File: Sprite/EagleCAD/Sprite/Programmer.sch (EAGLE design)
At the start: 5 parts

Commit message: Programmer Board
Finished programmer shield board
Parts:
- added JP5: (no value), SparkFun:M03LOCK
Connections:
- new net 3.3V: JP2.1, JP3.1
- new net GND: JP1.3, JP5.1, JP5.2
- new net RST: JP2.2, JP3.3
- new net RXD: JP2.3, JP4.1
- new net TEST: JP1.2, JP3.2
- new net TXD: JP1.1, JP3.4
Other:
- moved on the sheet: U$1
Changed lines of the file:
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@@
 <part name="JP3" library="SparkFun" deviceset="M05" device="LOCK"/>
 <part name="JP4" library="SparkFun" deviceset="M05" device="LOCK"/>
+<part name="VCC" library="SparkFun" deviceset="3.3V" device=""/>
+<part name="GND1" library="SparkFun" deviceset="GND" device=""/>
+<part name="JP5" library="SparkFun" deviceset="M03" device="LOCK"/>
+<part name="GND2" library="SparkFun" deviceset="GND" device=""/>
+<part name="VCC1" library="SparkFun" deviceset="3.3V" device=""/>
 </parts>
 <sheets>
@@
 </plain>
 <instances>
-<instance part="U$1" gate="G$1" x="73.66" y="48.26"/>
+<instance part="U$1" gate="G$1" x="66.04" y="60.96"/>
 <instance part="JP1" gate="G$1" x="121.92" y="45.72"/>
 <instance part="JP2" gate="G$1" x="116.84" y="45.72" rot="R180"/>
 <instance part="JP3" gate="G$1" x="129.54" y="86.36" rot="R90"/>
 <instance part="JP4" gate="G$1" x="129.54" y="81.28" rot="R270"/>
+<instance part="VCC" gate="G$1" x="96.52" y="48.26"/>
+<instance part="GND1" gate="1" x="142.24" y="53.34"/>
+<instance part="JP5" gate="G$1" x="187.96" y="60.96" rot="R180"/>
+<instance part="GND2" gate="1" x="175.26" y="55.88"/>
+<instance part="VCC1" gate="G$1" x="134.62" y="99.06"/>
 </instances>
 <busses>
 </busses>
 <nets>
+<net name="3.3V" class="0">
+<segment>
+<pinref part="JP2" gate="G$1" pin="1"/>
+<pinref part="VCC" gate="G$1" pin="3.3V"/>
+<wire x1="109.22" y1="48.26" x2="96.52" y2="48.26" width="0.1524" layer="91"/>
+</segment>
+<segment>
+<pinref part="JP3" gate="G$1" pin="1"/>
+<wire x1="134.62" y1="93.98" x2="134.62" y2="99.06" width="0.1524" layer="91"/>
+<pinref part="VCC1" gate="G$1" pin="3.3V"/>
+</segment>
+</net>
+<net name="RST" class="0">
+<segment>
+<pinref part="JP2" gate="G$1" pin="2"/>
+<wire x1="109.22" y1="45.72" x2="96.52" y2="45.72" width="0.1524" layer="91"/>
+<label x="96.52" y="45.72" size="1.778" layer="95" rot="R180"/>
+</segment>
+<segment>
+<pinref part="JP3" gate="G$1" pin="3"/>
+<wire x1="129.54" y1="93.98" x2="129.54" y2="99.06" width="0.1524" layer="91"/>
+<label x="129.54" y="99.06" size="1.778" layer="95" rot="R90"/>
+</segment>
+</net>
+<net name="GND" class="0">
+<segment>
+<pinref part="JP1" gate="G$1" pin="3"/>
+<wire x1="129.54" y1="48.26" x2="132.08" y2="48.26" width="0.1524" layer="91"/>
+<wire x1="132.08" y1="48.26" x2="132.08" y2="58.42" width="0.1524" layer="91"/>
+<pinref part="GND1" gate="1" pin="GND"/>
+<wire x1="132.08" y1="58.42" x2="142.24" y2="58.42" width="0.1524" layer="91"/>
+<wire x1="142.24" y1="58.42" x2="142.24" y2="55.88" width="0.1524" layer="91"/>
+</segment>
+<segment>
+<pinref part="JP5" gate="G$1" pin="2"/>
+<wire x1="180.34" y1="60.96" x2="175.26" y2="60.96" width="0.1524" layer="91"/>
+<wire x1="175.26" y1="60.96" x2="175.26" y2="63.5" width="0.1524" layer="91"/>
+<pinref part="JP5" gate="G$1" pin="1"/>
+<wire x1="180.34" y1="63.5" x2="175.26" y2="63.5" width="0.1524" layer="91"/>
+<pinref part="GND2" gate="1" pin="GND"/>
+<wire x1="175.26" y1="60.96" x2="175.26" y2="58.42" width="0.1524" layer="91"/>
+<junction x="175.26" y="60.96"/>
+<junction x="175.26" y="63.5"/>
+</segment>
+</net>
+<net name="TEST" class="0">
+<segment>
+<pinref part="JP1" gate="G$1" pin="2"/>
+<wire x1="129.54" y1="45.72" x2="142.24" y2="45.72" width="0.1524" layer="91"/>
+<label x="142.24" y="45.72" size="1.778" layer="95"/>
+</segment>
+<segment>
+<pinref part="JP3" gate="G$1" pin="2"/>
+<wire x1="132.08" y1="93.98" x2="132.08" y2="99.06" width="0.1524" layer="91"/>
+<label x="132.08" y="99.06" size="1.778" layer="95" rot="R90"/>
+</segment>
+</net>
+<net name="TXD" class="0">
+<segment>
+<pinref part="JP3" gate="G$1" pin="4"/>
+<wire x1="127" y1="93.98" x2="127" y2="99.06" width="0.1524" layer="91"/>
+<label x="127" y="99.06" size="1.778" layer="95" rot="R90"/>
+</segment>
+<segment>
+<pinref part="JP1" gate="G$1" pin="1"/>
+<wire x1="129.54" y1="43.18" x2="142.24" y2="43.18" width="0.1524" layer="91"/>
+<label x="142.24" y="43.18" size="1.778" layer="95"/>
+</segment>
+</net>
+<net name="RXD" class="0">
+<segment>
+<pinref part="JP4" gate="G$1" pin="1"/>
+<wire x1="124.46" y1="73.66" x2="124.46" y2="68.58" width="0.1524" layer="91"/>
+<label x="124.46" y="68.58" size="1.778" layer="95" rot="R270"/>
+</segment>
+<segment>
+<pinref part="JP2" gate="G$1" pin="3"/>
+<wire x1="109.22" y1="43.18" x2="96.52" y2="43.18" width="0.1524" layer="91"/>
+<label x="96.52" y="43.18" size="1.778" layer="95" rot="R180"/>
+</segment>
+</net>
 </nets>
 </sheet>

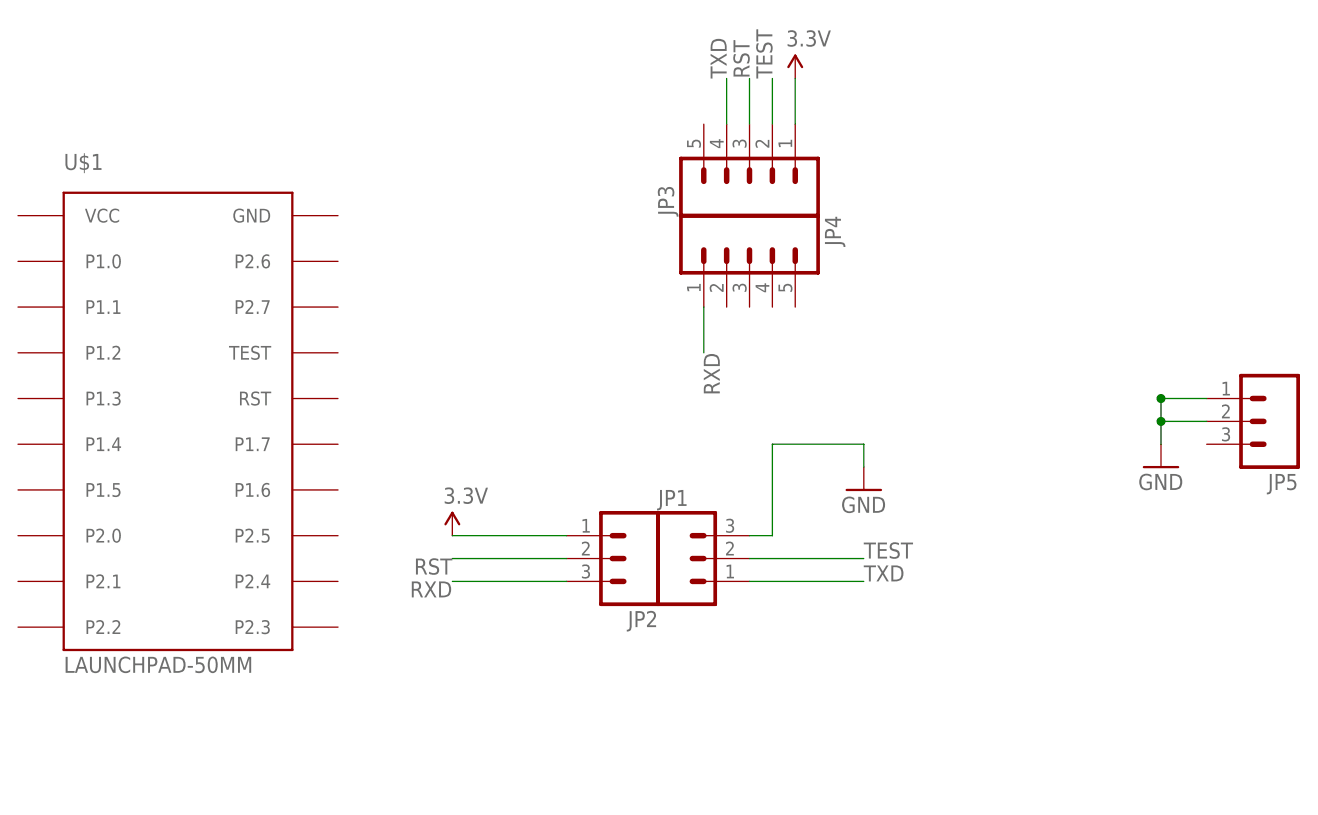
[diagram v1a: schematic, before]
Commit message: Finished Programmer Board
Added KickSat Silkscreen
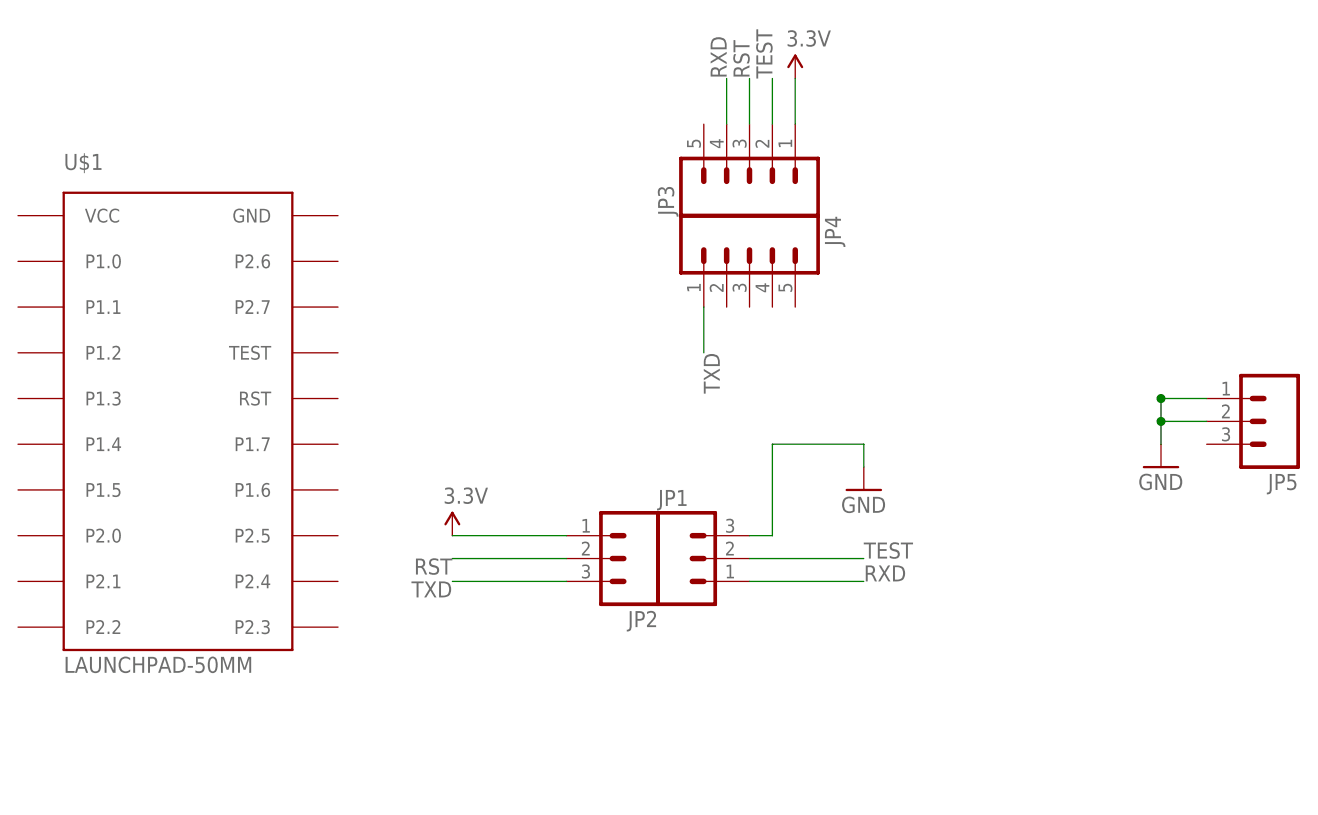
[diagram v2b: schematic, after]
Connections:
- net RXD: now also JP1.1, JP3.4; no longer JP2.3, JP4.1
- net TXD: now also JP2.3, JP4.1; no longer JP1.1, JP3.4
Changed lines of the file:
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@@
 </segment>
 </net>
-<net name="TXD" class="0">
+<net name="RXD" class="0">
 <segment>
 <pinref part="JP3" gate="G$1" pin="4"/>
@@
 </segment>
 </net>
-<net name="RXD" class="0">
+<net name="TXD" class="0">
 <segment>
 <pinref part="JP4" gate="G$1" pin="1"/>
